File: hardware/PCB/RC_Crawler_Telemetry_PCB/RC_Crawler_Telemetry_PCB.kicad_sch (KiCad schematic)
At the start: 0 parts

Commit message: Start KiCad telemetry PCB design
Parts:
- added J1: POWER_IN_5V, symbol Connector:Conn_01x02_Socket
- added J2: ESP32_LEFT, symbol Connector:Conn_01x15_Socket
- added J3: ESP32_right, symbol Connector:Conn_01x15_Socket
- added J4: BNO055_left, symbol Connector:Conn_01x06_Socket
- added J5: BNO055_right, symbol Connector:Conn_01x04_Socket

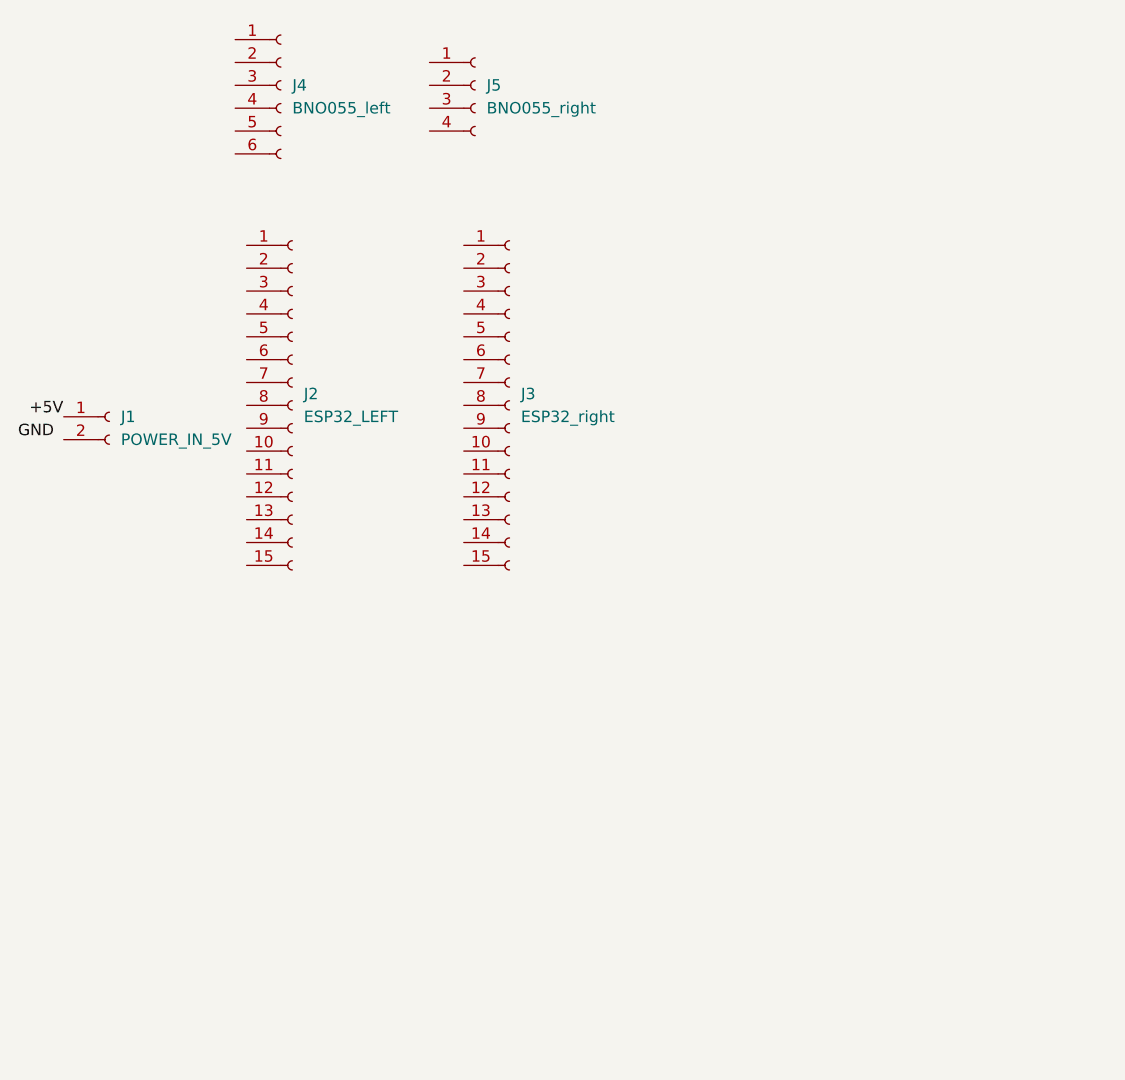
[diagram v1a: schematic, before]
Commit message: Add sensor interfaces and battery monitoring circuit
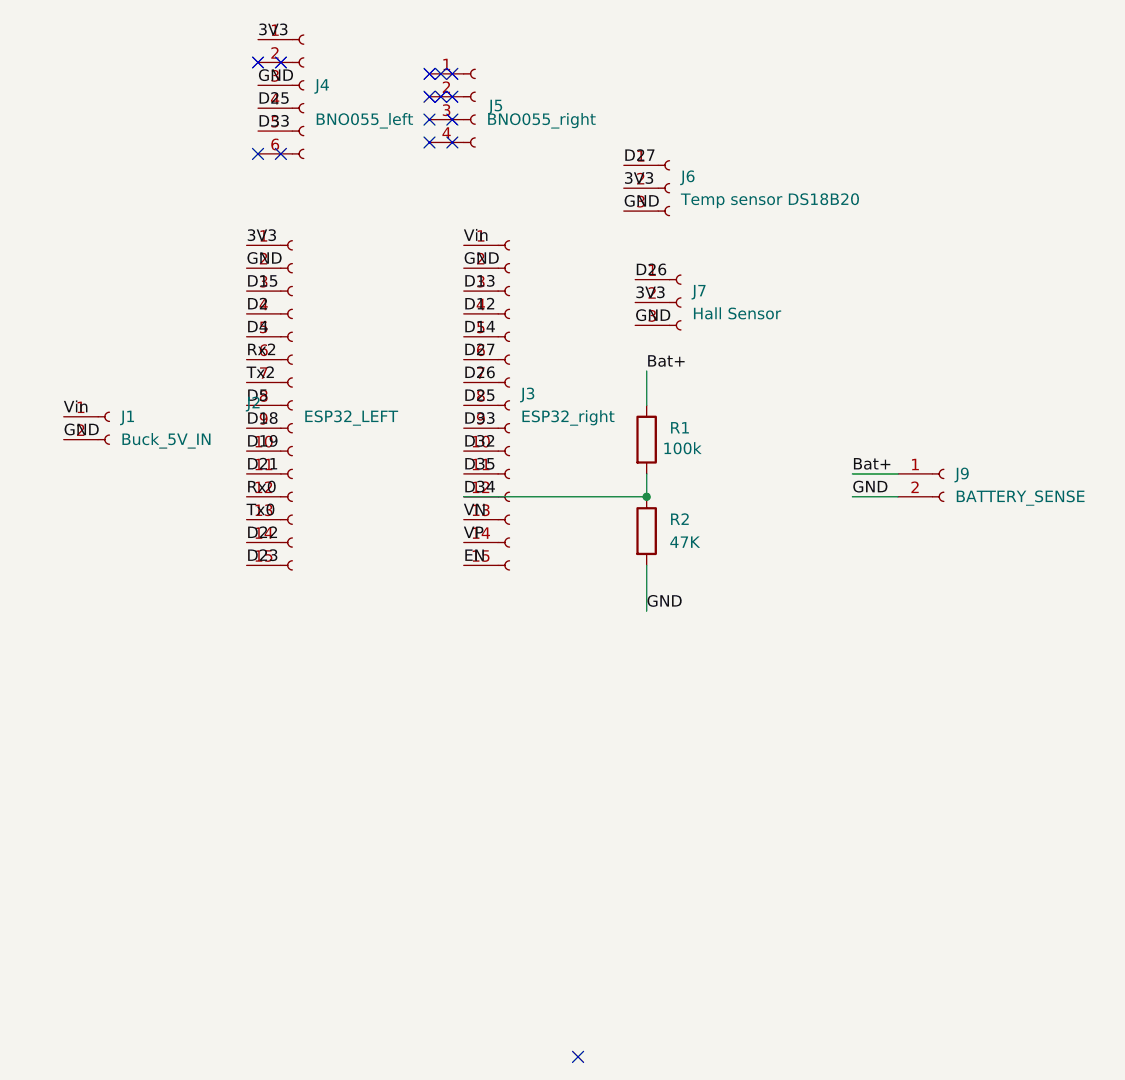
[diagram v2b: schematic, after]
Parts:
- added J6: Temp sensor DS18B20, symbol Connector:Conn_01x03_Socket
- added J7: Hall Sensor, symbol Connector:Conn_01x03_Socket
- added J9: BATTERY_SENSE, symbol Connector:Conn_01x02_Socket
- added R1: 100k, symbol Device:R
- added R2: 47K, symbol Device:R
- J1: value POWER_IN_5V -> Buck_5V_IN
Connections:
- net GND: now also J1.2 (Pin_2), J2.2 (Pin_2), J3.2 (Pin_2), J4.3 (Pin_3), J6.3 (Pin_3), J7.3 (Pin_3), J9.2 (Pin_2), R2.2
- net Vin: now reaches J3.1 (Pin_1)
- net Vin: now also J1.1 (Pin_1)
- net D32: now reaches J3.10 (Pin_10)
- net D35: now reaches J3.11 (Pin_11)
- net D34: now reaches J3.12 (Pin_12)
- net D34: now also R1.2, R2.1
- net VN: now reaches J3.13 (Pin_13)
- net VP: now reaches J3.14 (Pin_14)
- net EN: now reaches J3.15 (Pin_15)
- net D13: now reaches J3.3 (Pin_3)
- net D12: now reaches J3.4 (Pin_4)
- net D14: now reaches J3.5 (Pin_5)
- net D27: now reaches J3.6 (Pin_6)
- net D27: now also J6.1 (Pin_1)
- net D26: now reaches J3.7 (Pin_7)
- net D26: now also J7.1 (Pin_1)
- net D25: now reaches J3.8 (Pin_8)
- net D25: now also J4.4 (Pin_4)
- net D33: now reaches J3.9 (Pin_9)
- net D33: now also J4.5 (Pin_5)
- net 3V3: now reaches J4.1 (Pin_1)
- net 3V3: now also J2.1 (Pin_1), J6.2 (Pin_2), J7.2 (Pin_2)
- net D19: now reaches J2.10 (Pin_10)
- net D21: now reaches J2.11 (Pin_11)
- net Rx0: now reaches J2.12 (Pin_12)
- net Tx0: now reaches J2.13 (Pin_13)
- net D22: now reaches J2.14 (Pin_14)
- net D23: now reaches J2.15 (Pin_15)
- net D15: now reaches J2.3 (Pin_3)
- net D2: now reaches J2.4 (Pin_4)
- net D4: now reaches J2.5 (Pin_5)
- net Rx2: now reaches J2.6 (Pin_6)
- net Tx2: now reaches J2.7 (Pin_7)
- net D5: now reaches J2.8 (Pin_8)
- net D18: now reaches J2.9 (Pin_9)
- new net Bat+: J9.1 (Pin_1), R1.1
- no-connect marks 0 -> 15
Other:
- moved on the sheet: J4, J5

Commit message: Complete first revision of telemetry PCB
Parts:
- J1, J9: footprint (none) -> TerminalBlock_Phoenix:TerminalBlock_Phoenix_MKDS-1,5-2_1x02_P5.00mm_Horizontal
- J2, J3: footprint (none) -> Connector_PinSocket_2.54mm:PinSocket_1x15_P2.54mm_Vertical
- J4: footprint (none) -> Connector_PinSocket_2.54mm:PinSocket_1x06_P2.54mm_Vertical
- J5: footprint (none) -> Connector_PinSocket_2.54mm:PinSocket_1x04_P2.54mm_Vertical
- J6: footprint (none) -> Connector_PinSocket_2.54mm:PinSocket_1x03_P2.54mm_Vertical
- J7: footprint (none) -> TerminalBlock_Phoenix:TerminalBlock_Phoenix_MKDS-1,5-3_1x03_P5.00mm_Horizontal
- R1, R2: footprint (none) -> Resistor_THT:R_Axial_DIN0207_L6.3mm_D2.5mm_P7.62mm_Horizontal
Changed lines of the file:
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@@
 			)
 		)
-		(property "Footprint" ""
+		(property "Footprint" "Resistor_THT:R_Axial_DIN0207_L6.3mm_D2.5mm_P7.62mm_Horizontal"
 			(at 202.692 116.84 90)
 			(hide yes)
@@
 			)
 		)
-		(property "Footprint" ""
+		(property "Footprint" "TerminalBlock_Phoenix:TerminalBlock_Phoenix_MKDS-1,5-3_1x03_P5.00mm_Horizontal"
 			(at 208.28 91.44 0)
 			(hide yes)
@@
 			)
 		)
-		(property "Footprint" ""
+		(property "Footprint" "Resistor_THT:R_Axial_DIN0207_L6.3mm_D2.5mm_P7.62mm_Horizontal"
 			(at 202.692 106.68 90)
 			(hide yes)
@@
 			)
 		)
-		(property "Footprint" ""
+		(property "Footprint" "Connector_PinSocket_2.54mm:PinSocket_1x15_P2.54mm_Vertical"
 			(at 189.23 102.87 0)
 			(hide yes)
@@
 			)
 		)
-		(property "Footprint" ""
+		(property "Footprint" "TerminalBlock_Phoenix:TerminalBlock_Phoenix_MKDS-1,5-2_1x02_P5.00mm_Horizontal"
 			(at 237.49 110.49 0)
 			(hide yes)
@@
 			)
 		)
-		(property "Footprint" ""
+		(property "Footprint" "Connector_PinSocket_2.54mm:PinSocket_1x04_P2.54mm_Vertical"
 			(at 185.42 68.58 0)
 			(hide yes)
@@
 			)
 		)
-		(property "Footprint" ""
+		(property "Footprint" "TerminalBlock_Phoenix:TerminalBlock_Phoenix_MKDS-1,5-2_1x02_P5.00mm_Horizontal"
 			(at 144.78 104.14 0)
 			(hide yes)
@@
 			)
 		)
-		(property "Footprint" ""
+		(property "Footprint" "Connector_PinSocket_2.54mm:PinSocket_1x03_P2.54mm_Vertical"
 			(at 207.01 78.74 0)
 			(hide yes)
@@
 			)
 		)
-		(property "Footprint" ""
+		(property "Footprint" "Connector_PinSocket_2.54mm:PinSocket_1x06_P2.54mm_Vertical"
 			(at 166.37 67.31 0)
 			(hide yes)
@@
 			)
 		)
-		(property "Footprint" ""
+		(property "Footprint" "Connector_PinSocket_2.54mm:PinSocket_1x15_P2.54mm_Vertical"
 			(at 165.1 102.87 0)
 			(hide yes)
